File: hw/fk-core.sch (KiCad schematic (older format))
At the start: 110 parts, among them J1 RF-SMA-EDGE, J10 S2B-PH-SM4-TB, J11 RF-SMA-EDGE, J4 Conn_01x01, J5 Conn_01x03, J6 Conn_01x05, J7 CONN-HDR-2x5, J9 MICRO-USB, M1 MOUNT_HOLE, M3 MOUNT_HOLE, M4 MOUNT_HOLE, M6 MOUNT_HOLE, M7 MICROSD, Q1 2N7002LT1G, Q2 2N7002LT1G, Q3 2N7002LT1G, Q4 2N7002LT1G, SW1 SPNO, SW2 SPNO, U1 ATWINC1500-MR210PA, U10 FGPMMOPA6H, U11 MAX1704XX, U2 ATSAMD21G18A-AU, U3 RFM95W, U4 24AA02E64, U5 S25FL116K0XMFI041, U6 BQ24074RGTT, U7 PCF8523, U8 MCP1700T-3302E/MB, U9 ISL8541x, Y1 FC-135, Y2 FC-135

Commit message: Fix USB footprint with the oval drills.
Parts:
- J9: footprint RocketScreamKicadLibrary:MICRO-USB -> conservify:MICRO-USB

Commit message: Adding NFET for peripherals.
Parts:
- added J2: Conn_01x02, conservify:SJ_OPEN, symbol Conn_01x02
- added Q5: 2N7002LT1G, RocketScreamKicadLibrary:SOT-23, symbol MOSFET-N
- added R6: 10K, RocketScreamKicadLibrary:RES-0603, symbol RESISTOR
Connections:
- net labels added: PERIPH_EN, PERIPH_GND
- wire segments 401 -> 412
- no-connect marks 34 -> 33
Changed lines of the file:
@@
 $EndComp
 $Comp
-L GND #PWR035
-U 1 1 5A59621D
-P 9500 9600
-F 0 "#PWR035" H 9500 9350 50  0001 C CNN
-F 1 "GND" H 9500 9450 50  0001 C CNN
-F 2 "" H 9500 9600 60  0000 C CNN
-F 3 "" H 9500 9600 60  0000 C CNN
-	1    9500 9600
-	1    0    0    -1
-$EndComp
-$Comp
 L 3V3 #PWR036
 U 1 1 5A59621E
@@
 $EndComp
 $Comp
-L GND #PWR037
-U 1 1 5A59621F
-P 11300 9300
-F 0 "#PWR037" H 11300 9050 50  0001 C CNN
-F 1 "GND" H 11300 9150 50  0001 C CNN
-F 2 "" H 11300 9300 60  0000 C CNN
-F 3 "" H 11300 9300 60  0000 C CNN
-	1    11300 9300
-	1    0    0    -1
-$EndComp
-$Comp
 L RESISTOR R23
 U 1 1 5A596225
@@
 $EndComp
 $Comp
-L GND #PWR056
-U 1 1 5A596256
-P 5450 14600
-F 0 "#PWR056" H 5450 14350 50  0001 C CNN
-F 1 "GND" H 5450 14450 50  0001 C CNN
-F 2 "" H 5450 14600 60  0000 C CNN
-F 3 "" H 5450 14600 60  0000 C CNN
-	1    5450 14600
-	1    0    0    -1
-$EndComp
-$Comp
 L 3V3 #PWR057
 U 1 1 5A596257
@@
 $EndComp
 $Comp
-L GND #PWR061
-U 1 1 5A59625F
-P 1600 14300
-F 0 "#PWR061" H 1600 14050 50  0001 C CNN
-F 1 "GND" H 1600 14150 50  0001 C CNN
-F 2 "" H 1600 14300 60  0000 C CNN
-F 3 "" H 1600 14300 60  0000 C CNN
-	1    1600 14300
-	1    0    0    -1
-$EndComp
-$Comp
 L RESISTOR R2
 U 1 1 5A596260
@@
 $EndComp
 $Comp
-L GND #PWR062
-U 1 1 5A596261
-P 800 14050
-F 0 "#PWR062" H 800 13800 50  0001 C CNN
-F 1 "GND" H 800 13900 50  0001 C CNN
-F 2 "" H 800 14050 60  0000 C CNN
-F 3 "" H 800 14050 60  0000 C CNN
-	1    800  14050
-	1    0    0    -1
-$EndComp
-$Comp
 L RESISTOR R1
 U 1 1 5A596262
@@
 $EndComp
 $Comp
-L GND #PWR064
-U 1 1 5A596265
-P 4450 15550
-F 0 "#PWR064" H 4450 15300 50  0001 C CNN
-F 1 "GND" H 4450 15400 50  0001 C CNN
-F 2 "" H 4450 15550 60  0000 C CNN
-F 3 "" H 4450 15550 60  0000 C CNN
-	1    4450 15550
-	1    0    0    -1
-$EndComp
-$Comp
 L RESISTOR R5
 U 1 1 5A596266
@@
 	4850 3400 4550 3400
 Wire Wire Line
-	4850 3300 4550 3300
-Wire Wire Line
 	4850 3200 4550 3200
 Wire Wire Line
@@
 	9600 9500 9500 9500
 Wire Wire Line
-	9500 9500 9500 9600
+	9500 9500 9500 9950
 Wire Wire Line
 	11200 9200 11300 9200
 Wire Wire Line
-	11300 9200 11300 9300
+	11300 9200 11300 9950
 Wire Wire Line
 	9250 7450 9250 7550
@@
 	19200 8700 19200 8800
 Wire Wire Line
-	1600 14300 1600 14200
+	1600 14200 1600 15800
 Wire Wire Line
 	1600 12900 1600 13700
@@
 	800  12700 800  13250
 Wire Wire Line
-	800  14050 800  13750
+	800  13750 800  14300
 Wire Wire Line
 	4300 15200 4450 15200
 Wire Wire Line
-	4450 15200 4450 15550
+	4450 15200 4450 15800
 Wire Wire Line
 	4450 15400 4300 15400
@@
 Text Label 4550 2700 0    50   ~ 0
 D30
-NoConn ~ 4850 3300
 NoConn ~ 18200 2700
 NoConn ~ 10700 12250
@@
 	15550 14550 15550 14650
 Connection ~ 15550 14650
+$Comp
+L MOSFET-N Q5
+U 1 1 5AF09DFE
+P 13600 10200
+F 0 "Q5" H 13850 10250 50  0000 R CNN
+F 1 "2N7002LT1G" H 14200 10150 50  0000 R CNN
+F 2 "RocketScreamKicadLibrary:SOT-23" H 13600 9900 29  0001 C CNN
+F 3 "" H 13500 10200 60  0000 C CNN
+F 4 "0.14" H 13850 10350 50  0001 C CNN "price"
+F 5 "863-2N7002LT1G" H 11900 2850 50  0001 C CNN "spn1"
+F 6 "mouser" H 11900 2850 50  0001 C CNN "supplier1"
+	1    13600 10200
+	-1   0    0    -1
+$EndComp
+$Comp
+L RESISTOR R6
+U 1 1 5AF0C200
+P 14150 10500
+F 0 "R6" V 14150 10350 60  0000 C CNN
+F 1 "10K" V 14250 10350 60  0000 C CNN
+F 2 "RocketScreamKicadLibrary:RES-0603" H 14150 10300 60  0001 C CNN
+F 3 "" H 14150 10500 60  0000 C CNN
+F 4 "0.1" H 14150 10450 50  0001 C CNN "price"
+F 5 "603-RC0603FR-0710KL" H 2400 7200 50  0001 C CNN "spn1"
+F 6 "mouser" H 2400 7200 50  0001 C CNN "supplier1"
+	1    14150 10500
+	0    1    1    0
+$EndComp
+$Comp
+L GND #PWR094
+U 1 1 5AF0EFBB
+P 13600 10900
+F 0 "#PWR094" H 13600 10650 50  0001 C CNN
+F 1 "GND" H 13600 10750 50  0001 C CNN
+F 2 "" H 13600 10900 60  0000 C CNN
+F 3 "" H 13600 10900 60  0000 C CNN
+	1    13600 10900
+	1    0    0    -1
+$EndComp
+Wire Wire Line
+	13600 10450 13600 10900
+Wire Wire Line
+	13600 10850 15200 10850
+Wire Wire Line
+	14150 10850 14150 10750
+Connection ~ 13600 10850
+Wire Wire Line
+	14150 10250 14150 10200
+Wire Wire Line
+	13900 10200 14800 10200
+Connection ~ 14150 10200
+Text Label 14250 10200 0    60   ~ 0
+PERIPH_EN
+Text Label 14250 9950 0    60   ~ 0
+PERIPH_GND
+Wire Wire Line
+	13600 9950 15200 9950
+$Comp
+L Conn_01x02 J2
+U 1 1 5AF12C1F
+P 15400 9950
+F 0 "J2" H 15400 10050 50  0000 C CNN
+F 1 "Conn_01x02" H 15400 9750 50  0000 C CNN
+F 2 "conservify:SJ_OPEN" H 15400 9950 50  0001 C CNN
+F 3 "" H 15400 9950 50  0001 C CNN
+	1    15400 9950
+	1    0    0    -1
+$EndComp
+Wire Wire Line
+	15200 10850 15200 10050
+Connection ~ 14150 10850
+Text Label 4550 3300 0    60   ~ 0
+PERIPH_EN
+Wire Wire Line
+	4550 3300 5050 3300
+Text Label 9750 9950 0    60   ~ 0
+PERIPH_GND
+Wire Wire Line
+	11300 9950 9500 9950
+Text Label 5600 14600 0    60   ~ 0
+PERIPH_GND
+Wire Wire Line
+	5450 14600 6150 14600
+Text Label 2300 15800 0    60   ~ 0
+PERIPH_GND
+Wire Wire Line
+	4450 15800 1600 15800
+Wire Wire Line
+	800  14300 1600 14300
+Connection ~ 1600 14300
 $EndSCHEMATC

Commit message: Expose Vbus on the module connector.
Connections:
- wire segments 412 -> 411
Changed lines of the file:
@@
 	1200 9650 1350 9650
-Wire Wire Line
-	1350 9450 1200 9450
-Wire Wire Line
-	1200 9450 1200 9350
-Connection ~ 1200 9350
 Wire Wire Line
 	1350 9250 1200 9250
@@
 	800  14300 1600 14300
 Connection ~ 1600 14300
+$Comp
+L VBUS #PWR?
+U 1 1 5B28222B
+P 800 9450
+F 0 "#PWR?" H 800 9300 50  0001 C CNN
+F 1 "VBUS" H 800 9590 50  0000 C CNN
+F 2 "" H 800 9450 60  0000 C CNN
+F 3 "" H 800 9450 60  0000 C CNN
+	1    800  9450
+	1    0    0    -1
+$EndComp
+Wire Wire Line
+	1350 9450 800  9450
 $EndSCHEMATC

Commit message: Adding fiducials.
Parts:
- added M2, M5, M8: FIDUCIAL, RocketScreamKicadLibrary:FIDUCIAL-1MM, symbol FIDUCIAL
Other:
- note added: "FIDUCIALS"

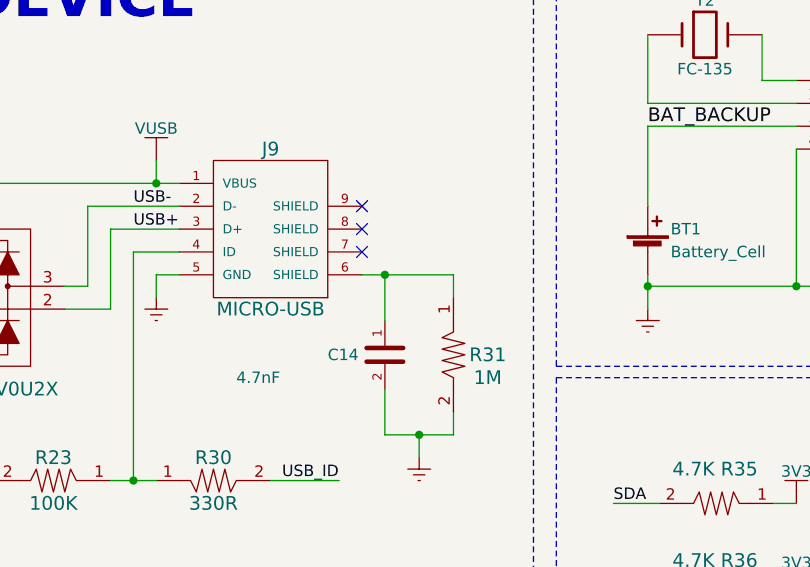
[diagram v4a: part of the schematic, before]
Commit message: Separate USB and SD a little more.
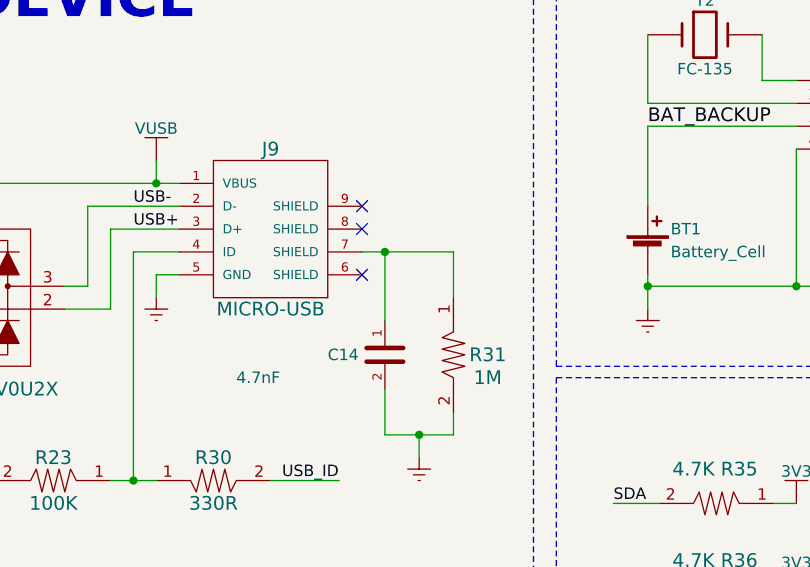
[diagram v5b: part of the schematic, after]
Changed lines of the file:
@@
 	4850 1650 4850 2100
 Wire Wire Line
-	11050 6650 11050 6850
+	11050 6550 11050 6850
 Wire Wire Line
 	8900 6250 10150 6250
@@
 	8200 2350 8400 2350
 Wire Wire Line
-	11350 6650 11350 6750
+	11350 6550 11350 6750
 Wire Notes Line
 	8800 8300 8800 10000
@@
 Wire Wire Line
 	15400 5800 15400 5700
-Wire Wire Line
-	10950 6650 11350 6650
-Connection ~ 11050 6650
-NoConn ~ 10950 6550
 $Comp
 L CAPACITOR-CERAMIC C1
@@
 Text Notes 3250 7000 0    180  ~ 36
 FIDUCIALS
+Wire Wire Line
+	10950 6550 11350 6550
+Connection ~ 11050 6550
+NoConn ~ 10950 6650
 $EndSCHEMATC
